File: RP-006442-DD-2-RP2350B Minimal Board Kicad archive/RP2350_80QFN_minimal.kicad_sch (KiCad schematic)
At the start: 49 parts, among them J1 USB_C_Receptacle_USB2.0_16P, J2 Conn_02x19_Odd_Even, J3 Conn_02x09_Odd_Even, SW1 SW_Push, SW2 SW_Push, U1 RP2350_80QFN, U2 NCP1117-3.3_SOT223, U3 W25Q128JVS, U4 DNF, Y1 ABM8-272-T3

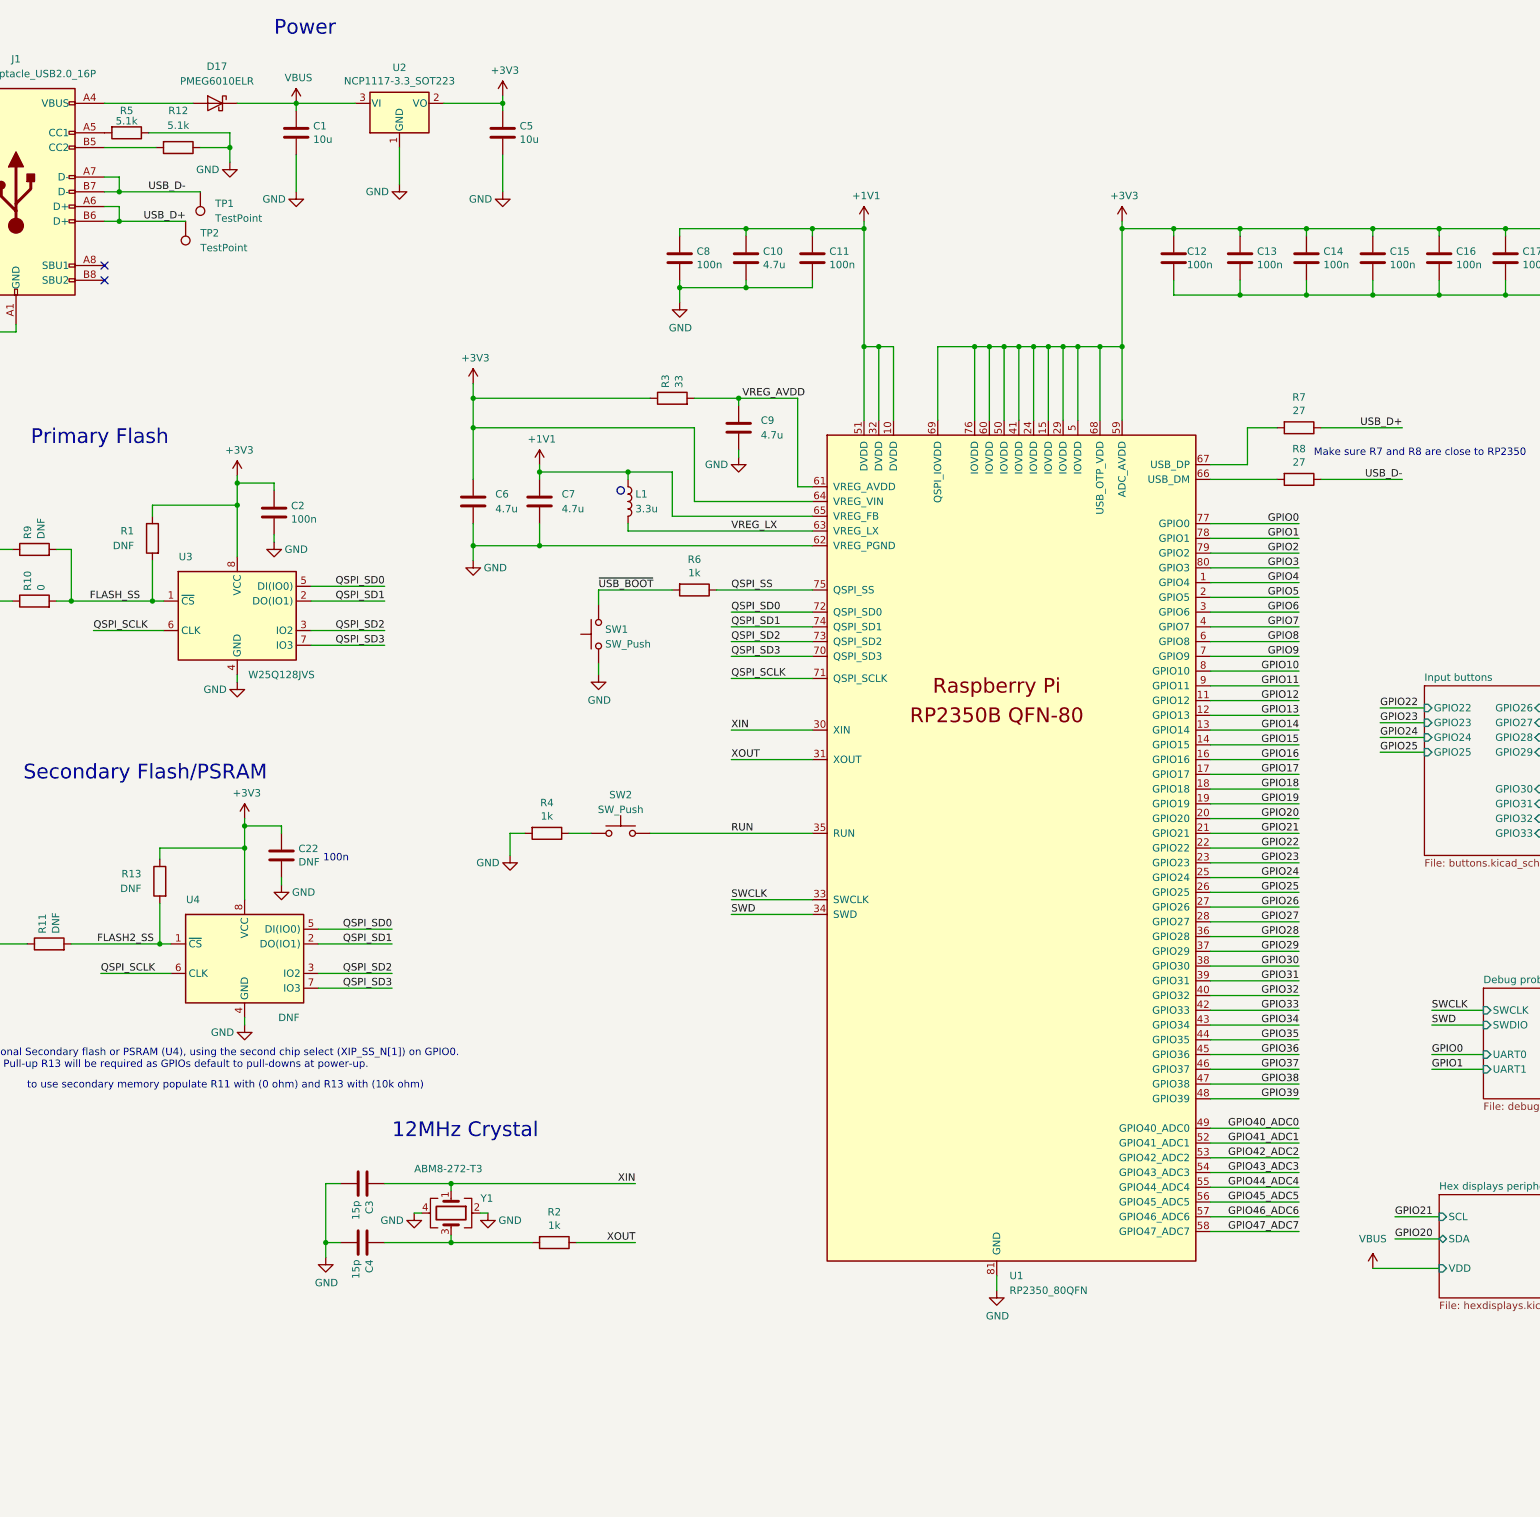
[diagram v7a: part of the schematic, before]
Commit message: Update to schematic and pcb
Changed:
- Added 100n decoupling capacitors to both 74HC595
- Changed ground plane to single common ground plane
- Added schottky diode to usb vbus inputs, creating separate vbus and vsys
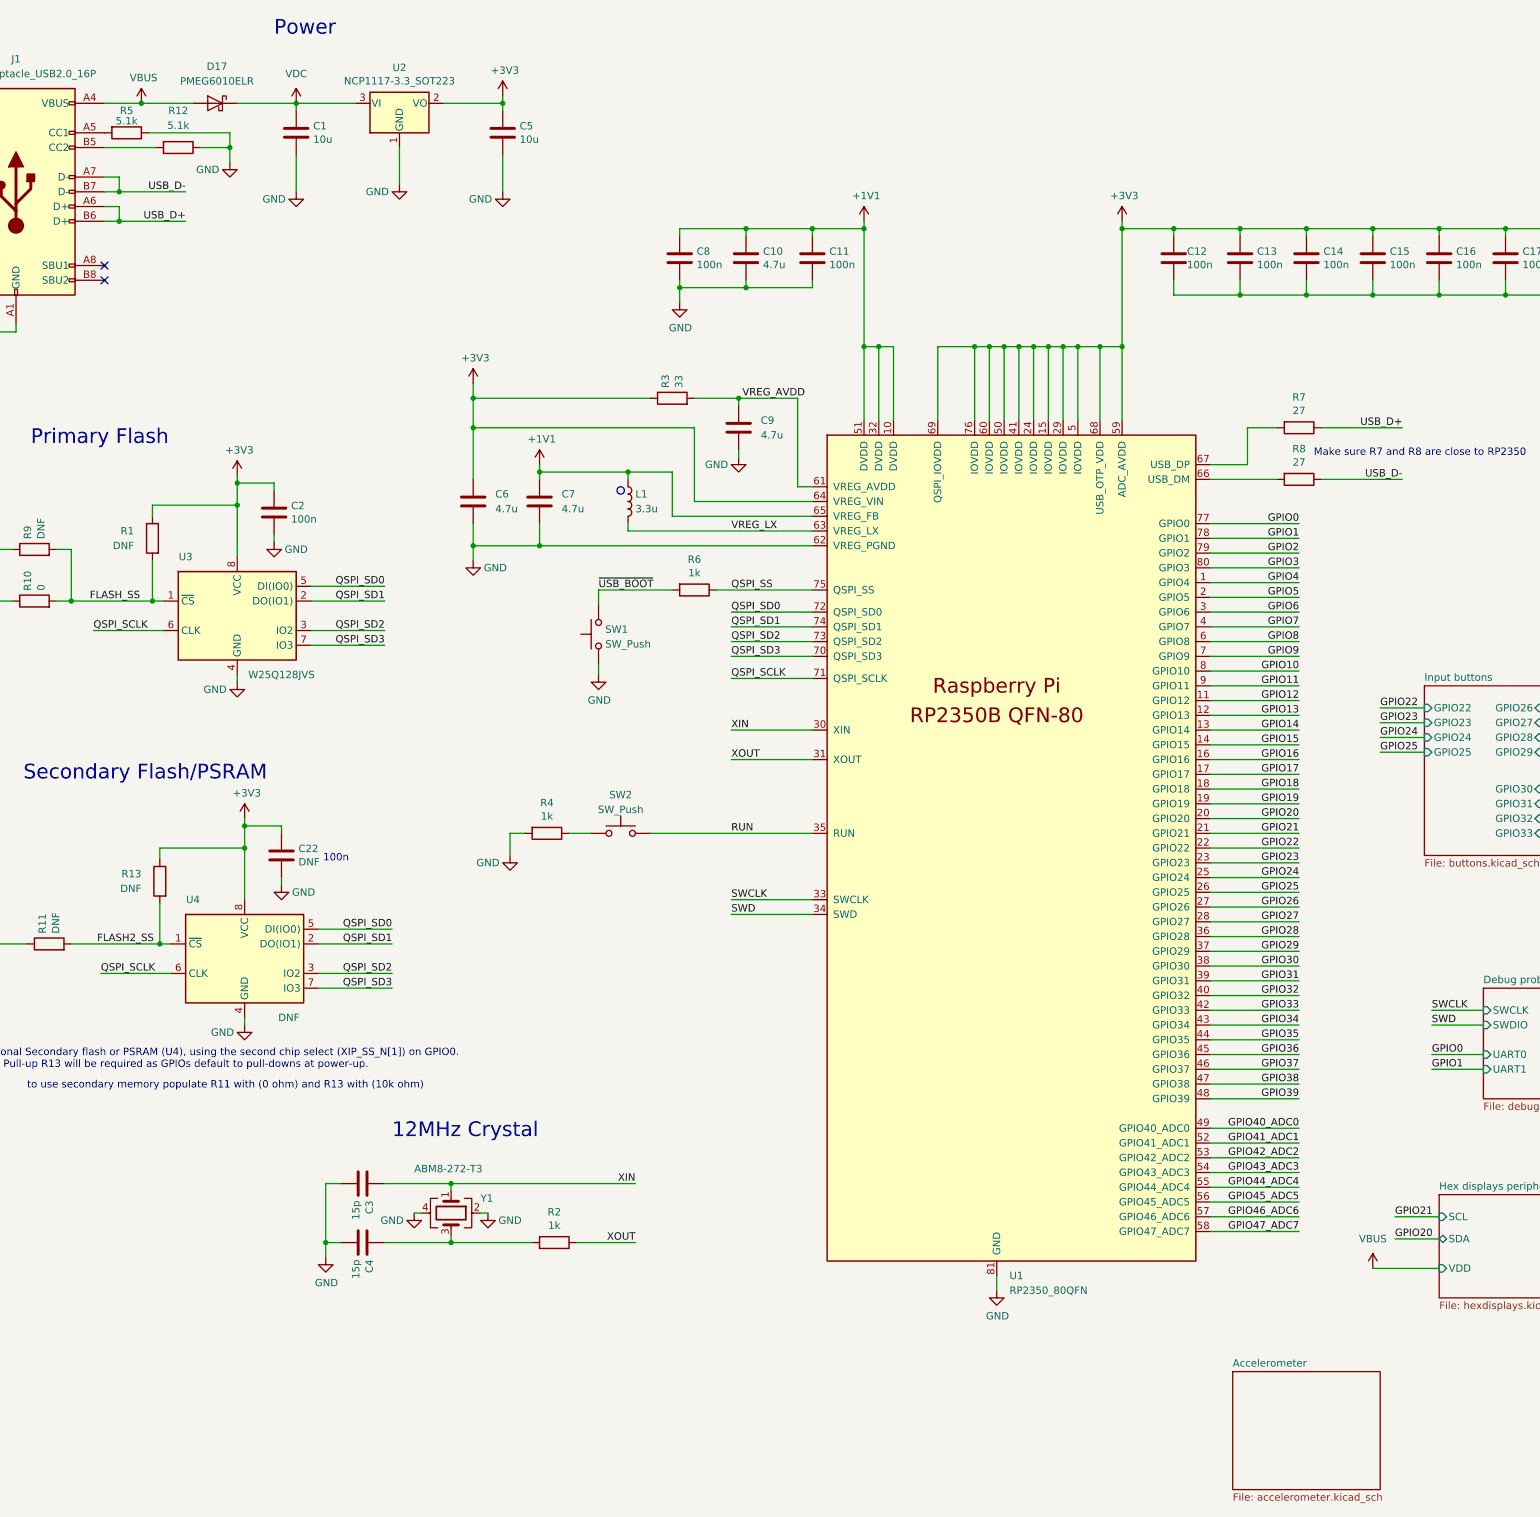
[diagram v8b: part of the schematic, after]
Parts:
- removed TP1, TP2: TestPoint, TestPoint:TestPoint_Pad_2.0x2.0mm, symbol Connector:TestPoint
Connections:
- net VBUS: now also D17.2 (A), J1.A4 (VBUS), J1.A9 (VBUS), J1.B4 (VBUS), J1.B9 (VBUS); no longer C1.1, D17.1 (K), U2.3 (VI)
- new net VDC: C1.1, D17.1 (K), U2.3 (VI)
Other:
- added sheet Accelerometer (accelerometer.kicad_sch)
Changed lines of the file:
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@@
 	)
 	(junction
-		(at 46.99 54.61)
-		(diameter 0)
-		(color 0 0 0 0)
-	)
-	(junction
 		(at 204.47 81.28)
 		(diameter 0)
@@
 	)
 	(junction
-		(at 322.58 100.33)
+		(at 46.99 54.61)
 		(diameter 0)
 		(color 0 0 0 0)
 	)
 	(junction
-		(at 104.14 225.425)
+		(at 322.58 100.33)
 		(diameter 0)
 		(color 0 0 0 0)
 	)
 	(junction
-		(at 77.47 39.37)
+		(at 104.14 225.425)
 		(diameter 0)
 		(color 0 0 0 0)
@@
 	)
 	(junction
+		(at 77.47 39.37)
+		(diameter 0)
+		(color 0 0 0 0)
+	)
+	(junction
+		(at 50.8 39.37)
+		(diameter 0)
+		(color 0 0 0 0)
+	)
+	(junction
 		(at 322.58 123.19)
 		(diameter 0)
@@
 	(wire
 		(pts
+			(xy 67.31 39.37) (xy 77.47 39.37)
+		)
+		(stroke
+			(width 0)
+			(type default)
+		)
+	)
+	(wire
+		(pts
 			(xy 262.89 62.23) (xy 262.89 60.96)
 		)
@@
 	(wire
 		(pts
-			(xy 46.99 54.61) (xy 60.96 54.61)
-		)
-		(stroke
-			(width 0)
-			(type default)
-		)
-	)
-	(wire
-		(pts
 			(xy 300.99 146.05) (xy 292.1 146.05)
 		)
@@
 	(wire
 		(pts
+			(xy 46.99 54.61) (xy 58.42 54.61)
+		)
+		(stroke
+			(width 0)
+			(type default)
+		)
+	)
+	(wire
+		(pts
 			(xy 336.55 130.81) (xy 349.25 130.81)
 		)
@@
 	(wire
 		(pts
-			(xy 67.31 39.37) (xy 77.47 39.37)
-		)
-		(stroke
-			(width 0)
-			(type default)
-		)
-	)
-	(wire
-		(pts
 			(xy 349.25 100.33) (xy 336.55 100.33)
 		)
@@
 	(wire
 		(pts
-			(xy 44.45 39.37) (xy 59.69 39.37)
+			(xy 44.45 39.37) (xy 50.8 39.37)
 		)
 		(stroke
@@
 	(wire
 		(pts
+			(xy 50.8 39.37) (xy 59.69 39.37)
+		)
+		(stroke
+			(width 0)
+			(type default)
+		)
+	)
+	(wire
+		(pts
 			(xy 234.95 195.58) (xy 250.19 195.58)
 		)
@@
 	(symbol
 		(lib_id "power:VBUS")
-		(at 77.47 39.37 0)
+		(at 50.8 39.37 0)
 		(unit 1)
 		(exclude_from_sim no)
@@
 		(dnp no)
 		(property "Reference" "#PWR02"
-			(at 77.47 43.18 0)
+			(at 50.8 43.18 0)
 			(effects
 				(font
@@
 		)
 		(property "Value" "VBUS"
-			(at 77.851 34.9758 0)
+			(at 51.181 34.9758 0)
 			(effects
 				(font
@@
 		)
 		(property "Footprint" ""
-			(at 77.47 39.37 0)
+			(at 50.8 39.37 0)
 			(effects
 				(font
@@
 		)
 		(property "Datasheet" ""
-			(at 77.47 39.37 0)
+			(at 50.8 39.37 0)
 			(effects
 				(font
@@
 		)
 		(property "Description" ""
-			(at 77.47 39.37 0)
+			(at 50.8 39.37 0)
 			(effects
 				(font
@@
 	)
 	(symbol
+		(lib_id "power:VDC")
+		(at 77.47 39.37 0)
+		(unit 1)
+		(exclude_from_sim no)
+		(in_bom yes)
+		(on_board yes)
+		(dnp no)
+		(fields_autoplaced yes)
+		(property "Reference" "#PWR071"
+			(at 77.47 43.18 0)
+			(effects
+				(font
+					(size 1.27 1.27)
+				)
+				(hide yes)
+			)
+		)
+		(property "Value" "VDC"
+			(at 77.47 34.29 0)
+			(effects
+				(font
+					(size 1.27 1.27)
+				)
+			)
+		)
+		(property "Footprint" ""
+			(at 77.47 39.37 0)
+			(effects
+				(font
+					(size 1.27 1.27)
+				)
+				(hide yes)
+			)
+		)
+		(property "Datasheet" ""
+			(at 77.47 39.37 0)
+			(effects
+				(font
+					(size 1.27 1.27)
+				)
+				(hide yes)
+			)
+		)
+		(property "Description" "Power symbol creates a global label with name \"VDC\""
+			(at 77.47 39.37 0)
+			(effects
+				(font
+					(size 1.27 1.27)
+				)
+				(hide yes)
+			)
+		)
+		(pin "1"
+		)
+		(instances
+			(project ""
+				(path "/94683f5c-9cd9-448e-be96-9792537b5cb8"
+					(reference "#PWR071")
+					(unit 1)
+				)
+			)
+		)
+	)
+	(symbol
 		(lib_id "power:GND")
 		(at 74.93 173.99 0)
@@
 	)
 	(symbol
-		(lib_id "Connector:TestPoint")
-		(at 58.42 59.69 180)
-		(unit 1)
-		(exclude_from_sim no)
-		(in_bom yes)
-		(on_board yes)
-		(dnp no)
-		(fields_autoplaced yes)
-		(property "Reference" "TP2"
-			(at 60.96 61.7219 0)
-			(effects
-				(font
-					(size 1.27 1.27)
-				)
-				(justify right)
-			)
-		)
-		(property "Value" "TestPoint"
-			(at 60.96 64.2619 0)
-			(effects
-				(font
-					(size 1.27 1.27)
-				)
-				(justify right)
-			)
-		)
-		(property "Footprint" "TestPoint:TestPoint_Pad_2.0x2.0mm"
-			(at 53.34 59.69 0)
-			(effects
-				(font
-					(size 1.27 1.27)
-				)
-				(hide yes)
-			)
-		)
-		(property "Datasheet" "~"
-			(at 53.34 59.69 0)
-			(effects
-				(font
-					(size 1.27 1.27)
-				)
-				(hide yes)
-			)
-		)
-		(property "Description" "test point"
-			(at 58.42 59.69 0)
-			(effects
-				(font
-					(size 1.27 1.27)
-				)
-				(hide yes)
-			)
-		)
-		(pin "1"
-		)
-		(instances
-			(project "RP2350_80QFN_minimal"
-				(path "/94683f5c-9cd9-448e-be96-9792537b5cb8"
-					(reference "TP2")
-					(unit 1)
-				)
-			)
-		)
-	)
-	(symbol
 		(lib_name "+3V3_1")
 		(lib_id "power:+3V3")
@@
 	)
 	(symbol
-		(lib_id "Connector:TestPoint")
-		(at 60.96 54.61 180)
-		(unit 1)
-		(exclude_from_sim no)
-		(in_bom yes)
-		(on_board yes)
-		(dnp no)
-		(fields_autoplaced yes)
-		(property "Reference" "TP1"
-			(at 63.5 56.6419 0)
-			(effects
-				(font
-					(size 1.27 1.27)
-				)
-				(justify right)
-			)
-		)
-		(property "Value" "TestPoint"
-			(at 63.5 59.1819 0)
-			(effects
-				(font
-					(size 1.27 1.27)
-				)
-				(justify right)
-			)
-		)
-		(property "Footprint" "TestPoint:TestPoint_Pad_2.0x2.0mm"
-			(at 55.88 54.61 0)
-			(effects
-				(font
-					(size 1.27 1.27)
-				)
-				(hide yes)
-			)
-		)
-		(property "Datasheet" "~"
-			(at 55.88 54.61 0)
-			(effects
-				(font
-					(size 1.27 1.27)
-				)
-				(hide yes)
-			)
-		)
-		(property "Description" "test point"
-			(at 60.96 54.61 0)
-			(effects
-				(font
-					(size 1.27 1.27)
-				)
-				(hide yes)
-			)
-		)
-		(pin "1"
-		)
-		(instances
-			(project ""
-				(path "/94683f5c-9cd9-448e-be96-9792537b5cb8"
-					(reference "TP1")
-					(unit 1)
-				)
-			)
-		)
-	)
-	(symbol
 		(lib_id "Device:R")
 		(at 146.05 123.19 270)
@@
 				)
 			)
+		)
+	)
+	(sheet
+		(at 238.76 257.81)
+		(size 25.4 20.32)
+		(exclude_from_sim no)
+		(in_bom yes)
+		(on_board yes)
+		(dnp no)
+		(fields_autoplaced yes)
+		(stroke
+			(width 0.1524)
+			(type solid)
+		)
+		(fill
+			(color 0 0 0 0.0000)
+		)
+		(property "Sheetname" "Accelerometer"
+			(at 238.76 257.0984 0)
+			(effects
+				(font
+					(size 1.27 1.27)
+				)
+				(justify left bottom)
+			)
+		)
+		(property "Sheetfile" "accelerometer.kicad_sch"
+			(at 238.76 278.7146 0)
+			(effects
+				(font
+					(size 1.27 1.27)
+				)
+				(justify left top)
+			)
+		)
+		(instances
+			(project "RP2350_80QFN_minimal"
+				(path "/94683f5c-9cd9-448e-be96-9792537b5cb8"
+					(page "6")
+				)
+			)
